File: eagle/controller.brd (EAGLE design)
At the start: 81.3 x 74.6 mm, 33 parts, among them K1 G5V1, T3 2N2222, T4 2N2222, X13 057-040-0

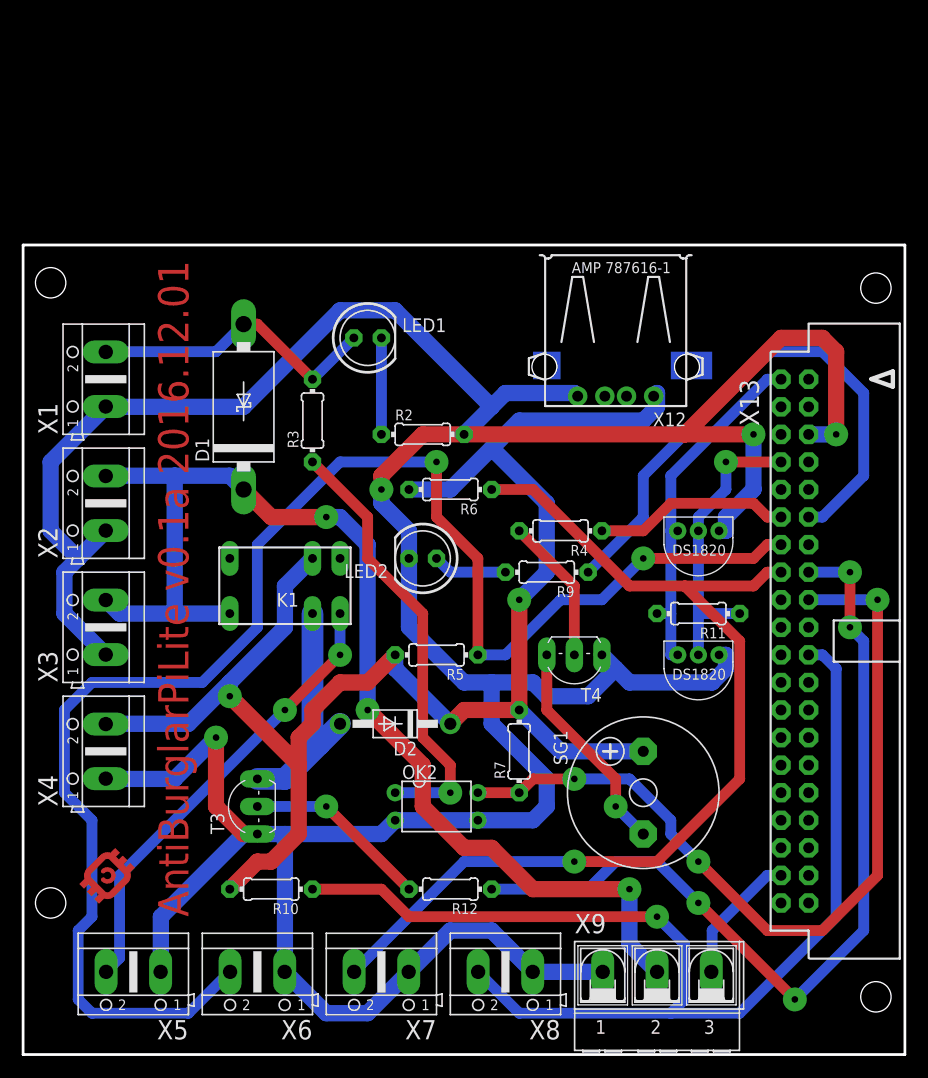
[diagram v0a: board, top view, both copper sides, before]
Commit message: Optimising board
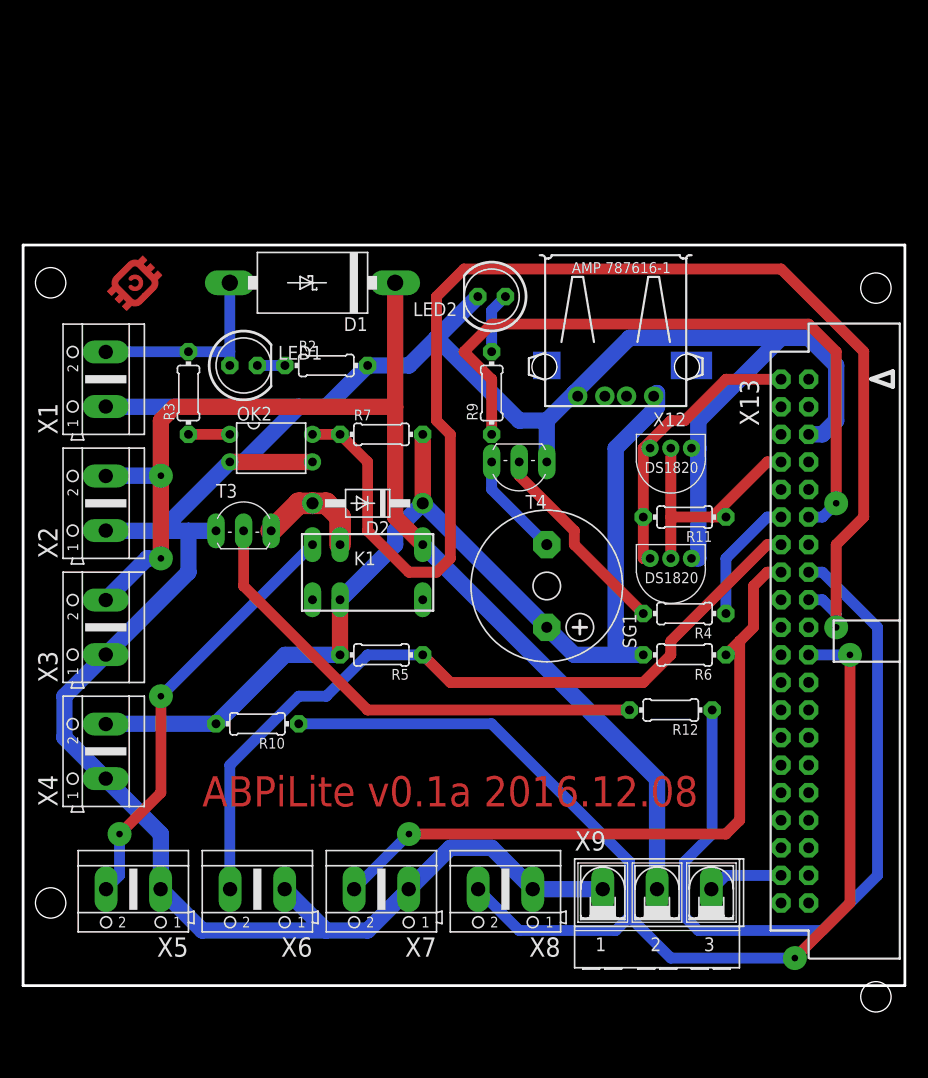
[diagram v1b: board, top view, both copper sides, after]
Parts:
- moved U$3 54.7 mm to (83.8, 105.4)
- moved OK2 36.4 mm to (96.5, 90.2)
- moved R7 31.9 mm to (106.7, 91.4), turned to 0 degrees
- moved T3 26.7 mm to (94.0, 83.8), turned to 0 degrees
- moved R6 26.4 mm to (134.6, 71.1)
- moved R12 26.2 mm to (133.3, 66.0)
- moved LED2 25.0 mm to (116.8, 104.1)
- moved SG1 21.0 mm to (121.9, 77.5), turned to 270 degrees
- moved D2 20.5 mm to (105.4, 85.1)
- moved T4 18.5 mm to (119.4, 87.6)
- moved R9 17.3 mm to (116.8, 95.2), turned to 90 degrees
- moved R10 15.3 mm to (95.2, 64.8)
- moved R4 13.7 mm to (134.6, 74.9)
- moved D1 13.1 mm to (100.3, 105.4), turned to 180 degrees
- moved R3 11.7 mm to (88.9, 95.2)
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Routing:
- net GND: track 344.1 -> 249.1 mm, vias 4 -> 0
- net N$13: track 144.1 -> 73.5 mm, vias 2 -> 0
- net N$22: track 151.3 -> 100.0 mm, vias 2 -> 0
- net N$9: track 77.7 -> 121.2 mm, vias 3 -> 1
- net N$8: track 40.8 -> 3.81 mm, vias 1 -> 0
- net N$15: track 93.7 -> 65.2 mm
- net N$2: track 17.1 -> 45.4 mm, vias 1 -> 0
- net N$3: track 22.1 -> 10.5 mm
- net N$11: track 20.2 -> 9.72 mm, vias 1 -> 0
- net N$17: track 51.9 -> 62.1 mm, vias 0 -> 1
- net N$21: track 80.6 -> 71.8 mm, vias 4 -> 0
- net N$1: track 27.6 -> 19.1 mm
- net N$6: track 18.1 -> 11.7 mm
- net N$7: track 8.89 -> 2.54 mm
- net N$20: track 32.9 -> 26.8 mm
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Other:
- board size 81.3 x 74.6 mm -> 81.3 x 68.2 mm
- board text added: "ABPiLite v0.1a 2016.12.08"
- board text removed: "AntiBurglarPiLite v0.1a 2016.12.01"
